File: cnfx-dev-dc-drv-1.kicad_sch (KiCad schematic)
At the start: 38 parts, among them J1 TC2030, J2 Conn_01x02, J3 Conn_01x04_Pin, J4 Conn_01x02, SW1 SW_Push, SW2 SW_Push, SW3 SW_Push, U1 SN65HVD230, U2 STM32F103C8Tx, Y1 8M

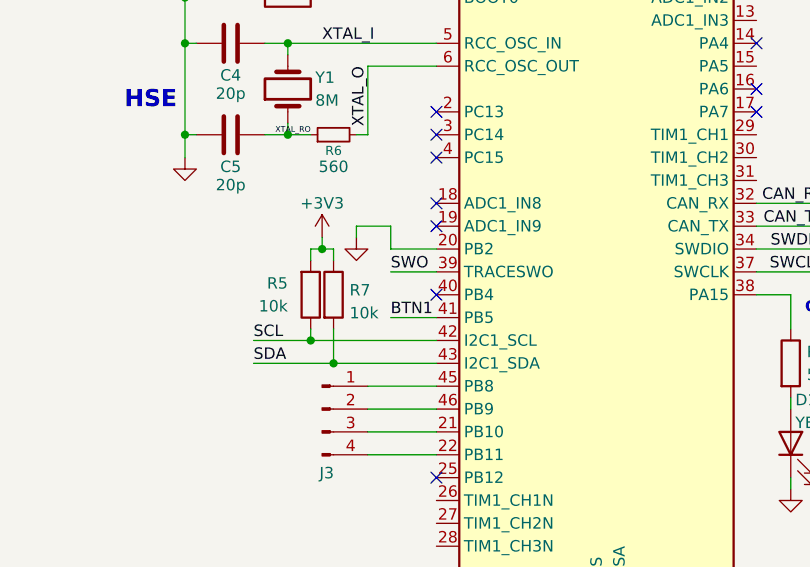
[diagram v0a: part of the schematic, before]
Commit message: schem: remove unused i2c pullups
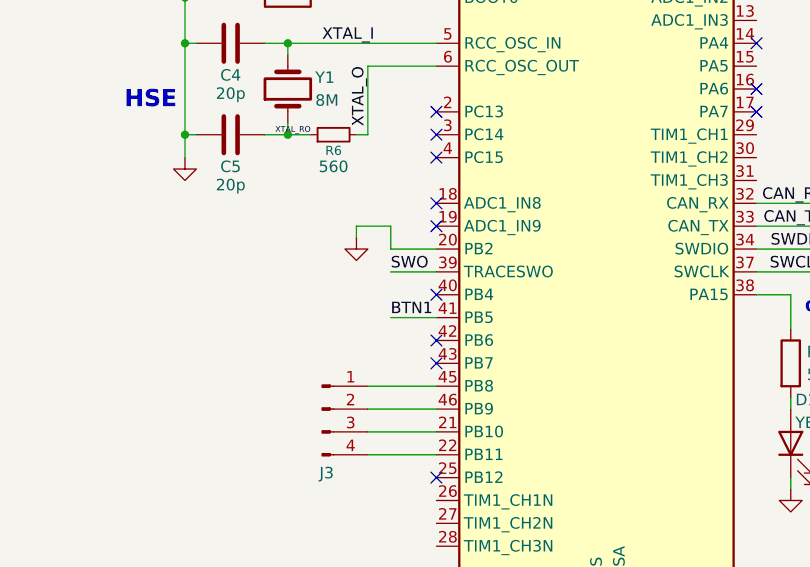
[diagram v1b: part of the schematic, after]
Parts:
- removed R5, R7: 10k, Resistor_SMD:R_0402_1005Metric, symbol Device:R
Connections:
- net SCL: no longer names the net of U2.42 (PB6)
- net SDA: no longer names the net of U2.43 (PB7)
- no-connect marks 13 -> 15

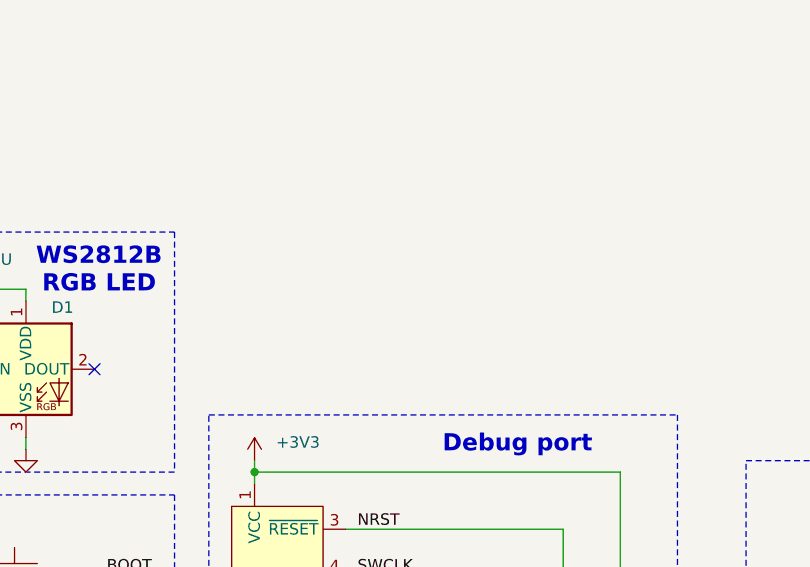
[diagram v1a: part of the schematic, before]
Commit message: schem: import HT753-1 3V3 100mA LDO
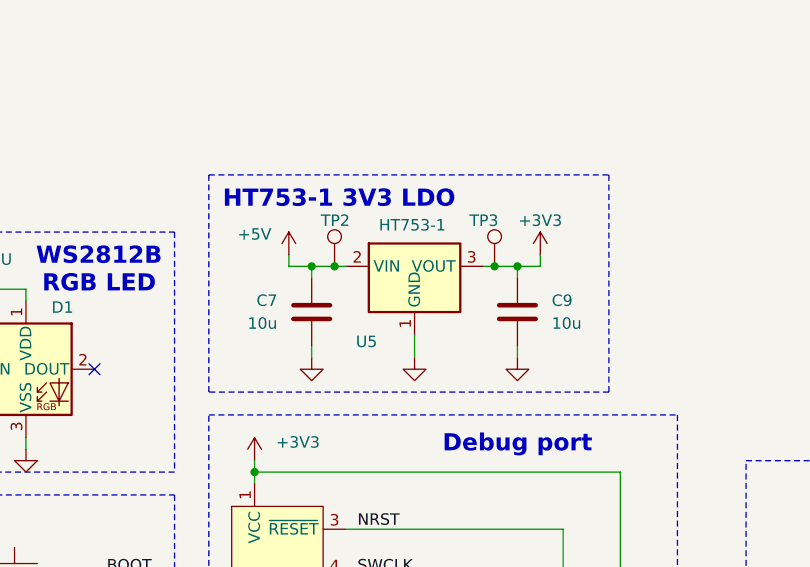
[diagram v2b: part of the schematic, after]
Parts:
- added C7, C9: 10u, Capacitor_SMD:C_0805_2012Metric, symbol Device:C
- added TP2, TP3: TestPoint, TestPoint:TestPoint_Pad_D2.0mm, symbol Connector:TestPoint
- added U5: HT753-1, Package_TO_SOT_SMD:SOT-89-3, symbol Regulator_Linear:HT75xx-1-SOT89
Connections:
- net +3V3: now also C9.1, TP3.1, U5.3 (VOUT)
- net GND: now also C7.2, C9.2, U5.1 (GND)
- new net +5V: C7.1, TP2.1, U5.2 (VIN)
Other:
- note added: "HT753-1 3V3 LDO"

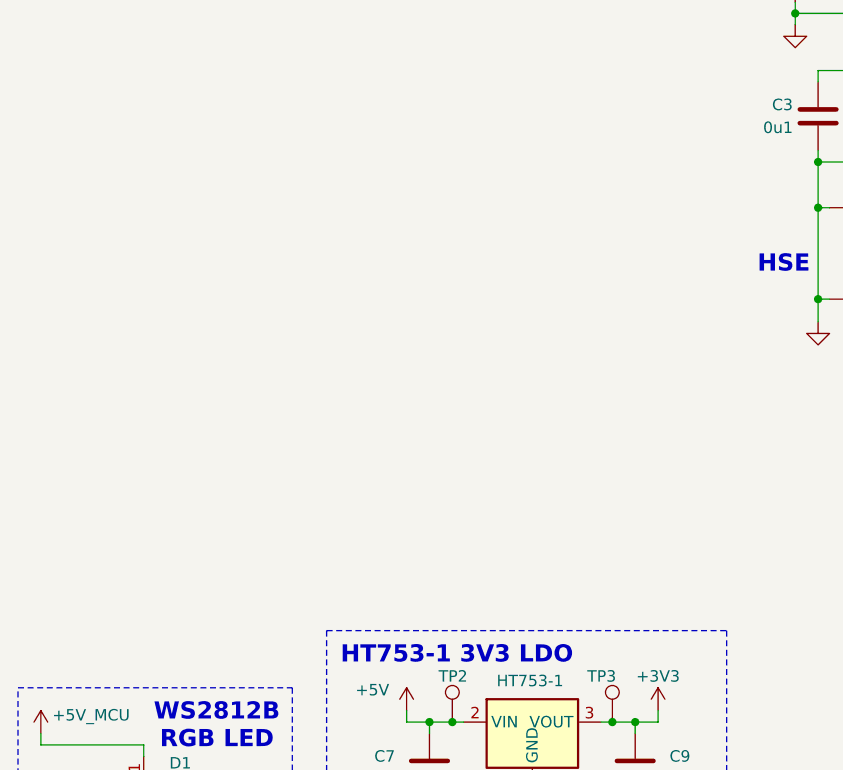
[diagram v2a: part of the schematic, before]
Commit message: schem: add TPS259472 5V 4A efuse
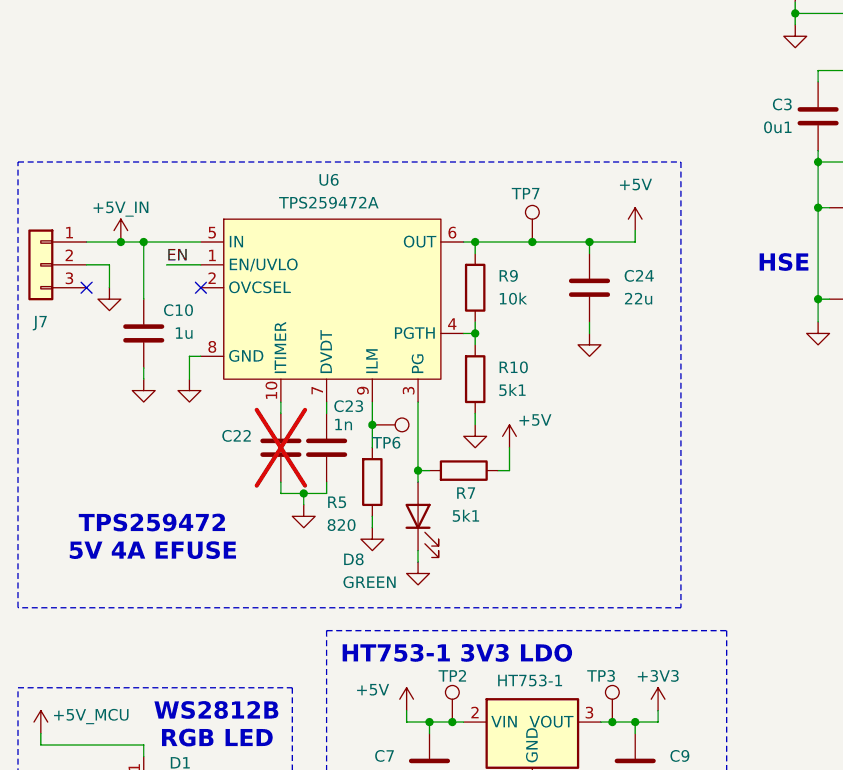
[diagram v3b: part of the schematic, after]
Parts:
- added C10: 1u, Capacitor_SMD:C_0402_1005Metric, symbol Device:C
- added C22: C, Capacitor_SMD:C_0402_1005Metric, symbol Device:C
- added C23: 1n, Capacitor_SMD:C_0402_1005Metric, symbol Device:C
- added C24: 22u, Capacitor_SMD:C_0402_1005Metric, symbol Device:C
- added D8: GREEN, LED_SMD:LED_0805_2012Metric, symbol Device:LED
- added J7: Conn_01x03, Connector_JST:JST_XH_B3B-XH-A_1x03_P2.50mm_Vertical, symbol Connector_Generic:Conn_01x03
- added R10, R7: 5k1, Resistor_SMD:R_0402_1005Metric, symbol Device:R
- added R5: 820, Resistor_SMD:R_0402_1005Metric, symbol Device:R
- added R9: 10k, Resistor_SMD:R_0402_1005Metric, symbol Device:R
- added TP6, TP7: TestPoint, GLCS:TestPoint_Keystone_5015_Micro_Mini, symbol Connector:TestPoint
- added U6: TPS259472A, GLCS:Texas_RPW0010A_VQFN-HR-10_2x2mm_P0.5mm, symbol GLCS:TPS259472x
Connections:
- net +5V: now also C24.1, R7.1, R9.2, TP7.1, U6.6 (OUT)
- net GND: now also C10.1, C22.2, C23.2, C24.2, D8.1 (K), J7.2 (Pin_2), R10.1, R5.1, U6.8 (GND)
- new net: R5.2, TP6.1, U6.9 (ILM)
- new net: C23.1, U6.7 (DVDT)
- new net: D8.2 (A), R7.2, U6.3 (PG)
- new net: C22.1, U6.10 (ITIMER)
- new net: R10.2, R9.1, U6.4 (PGTH)
- new net +5V_IN: C10.2, J7.1 (Pin_1), U6.5 (IN)
- new net EN: U6.1 (EN/UVLO)
- no-connect marks 15 -> 17
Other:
- note added: "TPS259472 5V 4A EFUSE"

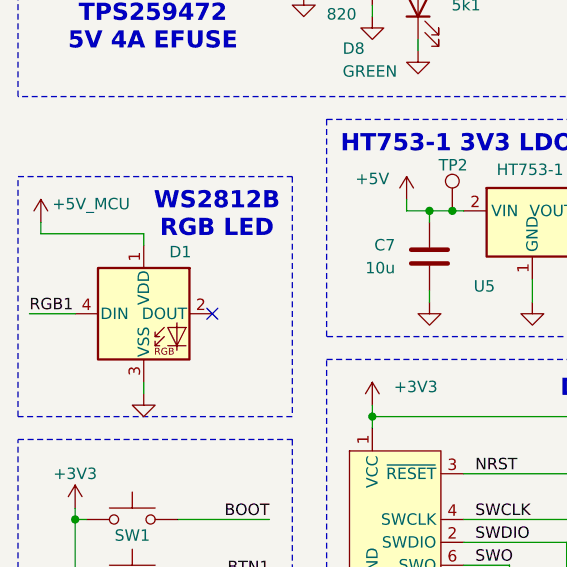
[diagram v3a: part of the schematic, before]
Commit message: schem: change rgb led +5V supply
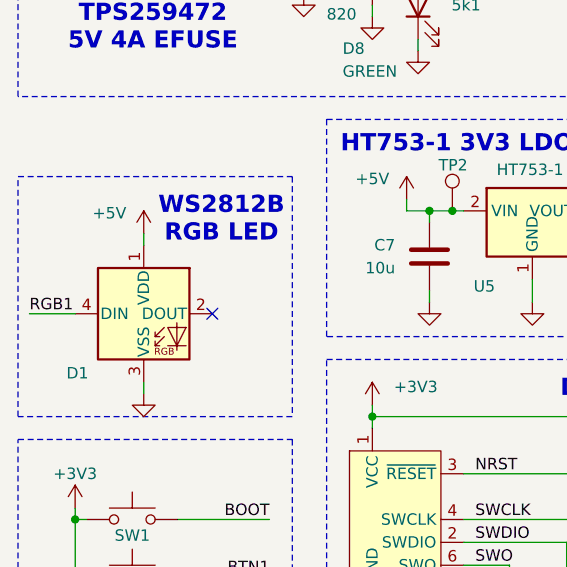
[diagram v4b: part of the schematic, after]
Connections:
- net +5V_MCU is gone; now on net +5V: D1.1 (VDD)
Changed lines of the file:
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@@
 	(text "WS2812B\nRGB LED"
 		(exclude_from_sim no)
-		(at 39.878 140.208 0)
+		(at 40.386 140.716 0)
 		(effects
 			(font
@@
 	(wire
 		(pts
-			(xy 20.32 142.24) (xy 31.75 142.24)
-		)
-		(stroke
-			(width 0)
-			(type default)
-		)
-	)
-	(wire
-		(pts
 			(xy 154.94 50.8) (xy 144.78 50.8)
 		)
@@
 	(wire
 		(pts
-			(xy 20.32 140.97) (xy 20.32 142.24)
-		)
-		(stroke
-			(width 0)
-			(type default)
-		)
-	)
-	(wire
-		(pts
 			(xy 165.1 55.88) (xy 165.1 63.5)
 		)
@@
 	)
 	(symbol
-		(lib_id "power:+5V")
-		(at 20.32 140.97 0)
-		(mirror y)
-		(unit 1)
-		(body_style 1)
-		(exclude_from_sim no)
-		(in_bom yes)
-		(on_board yes)
-		(in_pos_files yes)
-		(dnp no)
-		(property "Reference" "#PWR01"
-			(at 20.32 144.78 0)
-			(hide yes)
-			(show_name no)
-			(do_not_autoplace no)
-			(effects
-				(font
-					(size 1.27 1.27)
-				)
-			)
-		)
-		(property "Value" "+5V_MCU"
-			(at 25.908 138.938 0)
-			(show_name no)
-			(do_not_autoplace no)
-			(effects
-				(font
-					(size 1.27 1.27)
-				)
-			)
-		)
-		(property "Footprint" ""
-			(at 20.32 140.97 0)
-			(hide yes)
-			(show_name no)
-			(do_not_autoplace no)
-			(effects
-				(font
-					(size 1.27 1.27)
-				)
-			)
-		)
-		(property "Datasheet" ""
-			(at 20.32 140.97 0)
-			(hide yes)
-			(show_name no)
-			(do_not_autoplace no)
-			(effects
-				(font
-					(size 1.27 1.27)
-				)
-			)
-		)
-		(property "Description" "Power symbol creates a global label with name \"+5V\""
-			(at 20.32 140.97 0)
-			(hide yes)
-			(show_name no)
-			(do_not_autoplace no)
-			(effects
-				(font
-					(size 1.27 1.27)
-				)
-			)
-		)
-		(pin "1"
-		)
-		(instances
-			(project "cnfx-dev-dc-drv-1"
-				(path "/d7250a19-615d-468e-abbc-0dea4b78aeef"
-					(reference "#PWR01")
-					(unit 1)
-				)
-			)
-		)
-	)
-	(symbol
 		(lib_id "Device:C")
 		(at 111.76 92.71 270)
@@
 	)
 	(symbol
+		(lib_id "power:+5V")
+		(at 31.75 142.24 0)
+		(unit 1)
+		(body_style 1)
+		(exclude_from_sim no)
+		(in_bom yes)
+		(on_board yes)
+		(in_pos_files yes)
+		(dnp no)
+		(property "Reference" "#PWR037"
+			(at 31.75 146.05 0)
+			(hide yes)
+			(show_name no)
+			(do_not_autoplace no)
+			(effects
+				(font
+					(size 1.27 1.27)
+				)
+			)
+		)
+		(property "Value" "+5V"
+			(at 27.94 139.954 0)
+			(show_name no)
+			(do_not_autoplace no)
+			(effects
+				(font
+					(size 1.27 1.27)
+				)
+			)
+		)
+		(property "Footprint" ""
+			(at 31.75 142.24 0)
+			(hide yes)
+			(show_name no)
+			(do_not_autoplace no)
+			(effects
+				(font
+					(size 1.27 1.27)
+				)
+			)
+		)
+		(property "Datasheet" ""
+			(at 31.75 142.24 0)
+			(hide yes)
+			(show_name no)
+			(do_not_autoplace no)
+			(effects
+				(font
+					(size 1.27 1.27)
+				)
+			)
+		)
+		(property "Description" "Power symbol creates a global label with name \"+5V\""
+			(at 31.75 142.24 0)
+			(hide yes)
+			(show_name no)
+			(do_not_autoplace no)
+			(effects
+				(font
+					(size 1.27 1.27)
+				)
+			)
+		)
+		(pin "1"
+		)
+		(instances
+			(project "cnfx-dev-dc-drv-1"
+				(path "/d7250a19-615d-468e-abbc-0dea4b78aeef"
+					(reference "#PWR037")
+					(unit 1)
+				)
+			)
+		)
+	)
+	(symbol
 		(lib_id "Device:C")
 		(at 111.76 82.55 270)
@@
 		(dnp no)
 		(property "Reference" "D1"
-			(at 35.814 144.272 0)
+			(at 24.384 157.734 0)
 			(show_name no)
 			(do_not_autoplace no)

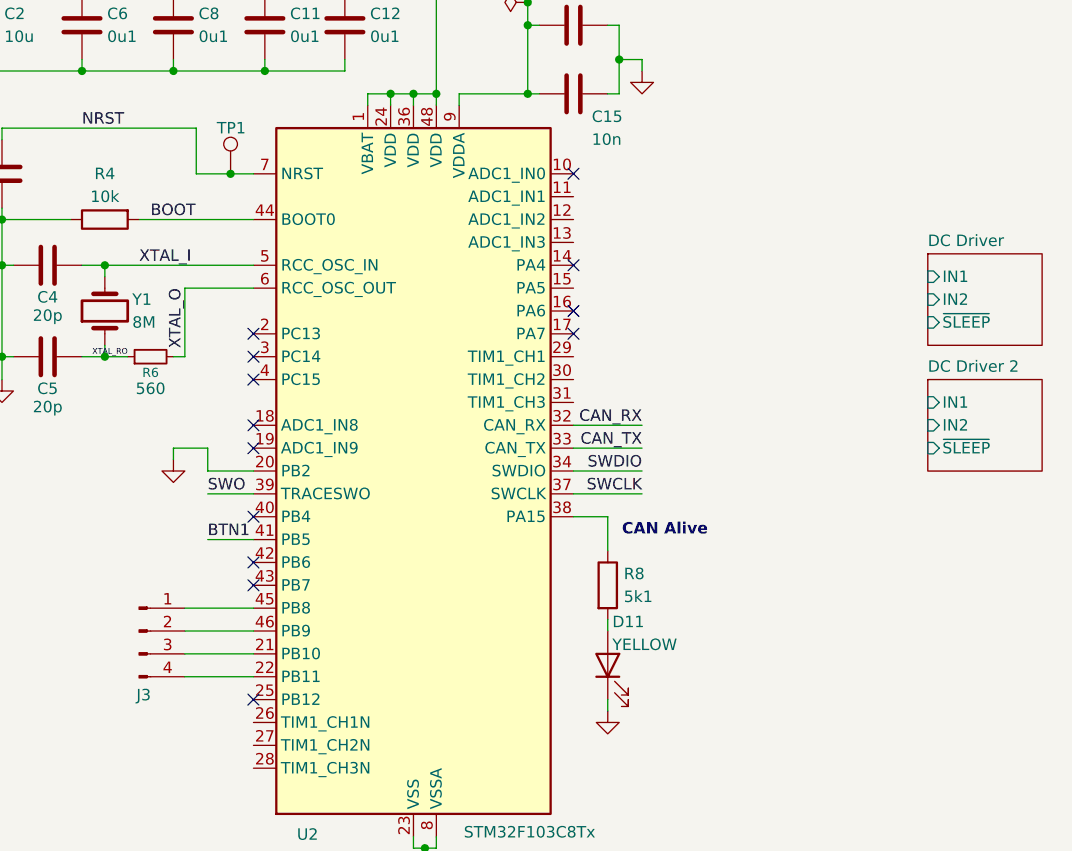
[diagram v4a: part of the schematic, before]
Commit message: schem: add UART connector
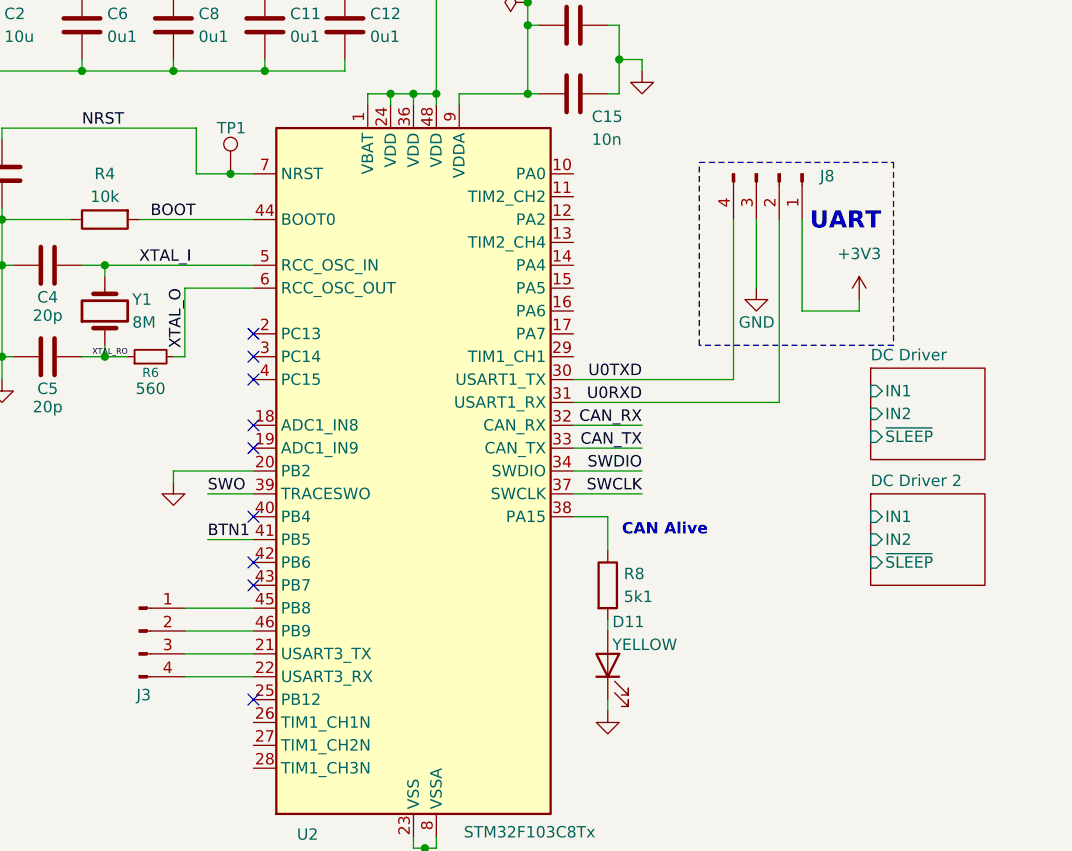
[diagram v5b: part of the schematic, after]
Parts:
- added J8: Conn_01x04_Pin, Connector_PinHeader_2.54mm:PinHeader_1x04_P2.54mm_Vertical, symbol Connector:Conn_01x04_Pin
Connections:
- net +3V3: now also J8.1 (Pin_1)
- net GND: now also J8.3 (Pin_3)
- net U0TXD: now reaches U2.30 (PA9)
- net U0TXD: now also J8.4 (Pin_4)
- net U0RXD: now reaches U2.31 (PA10)
- net U0RXD: now also J8.2 (Pin_2)
- no-connect marks 17 -> 13
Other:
- note added: "UART"
